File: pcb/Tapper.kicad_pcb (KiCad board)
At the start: 2 copper layers, 87.1 x 56 mm, 61 parts, among them J1 Barrel_Jack, J2 Conn_01x06_MountingPin, J3 Conn_01x06_MountingPin, J4 Conn_01x06_MountingPin, J5 Conn_01x14, U1 L7805

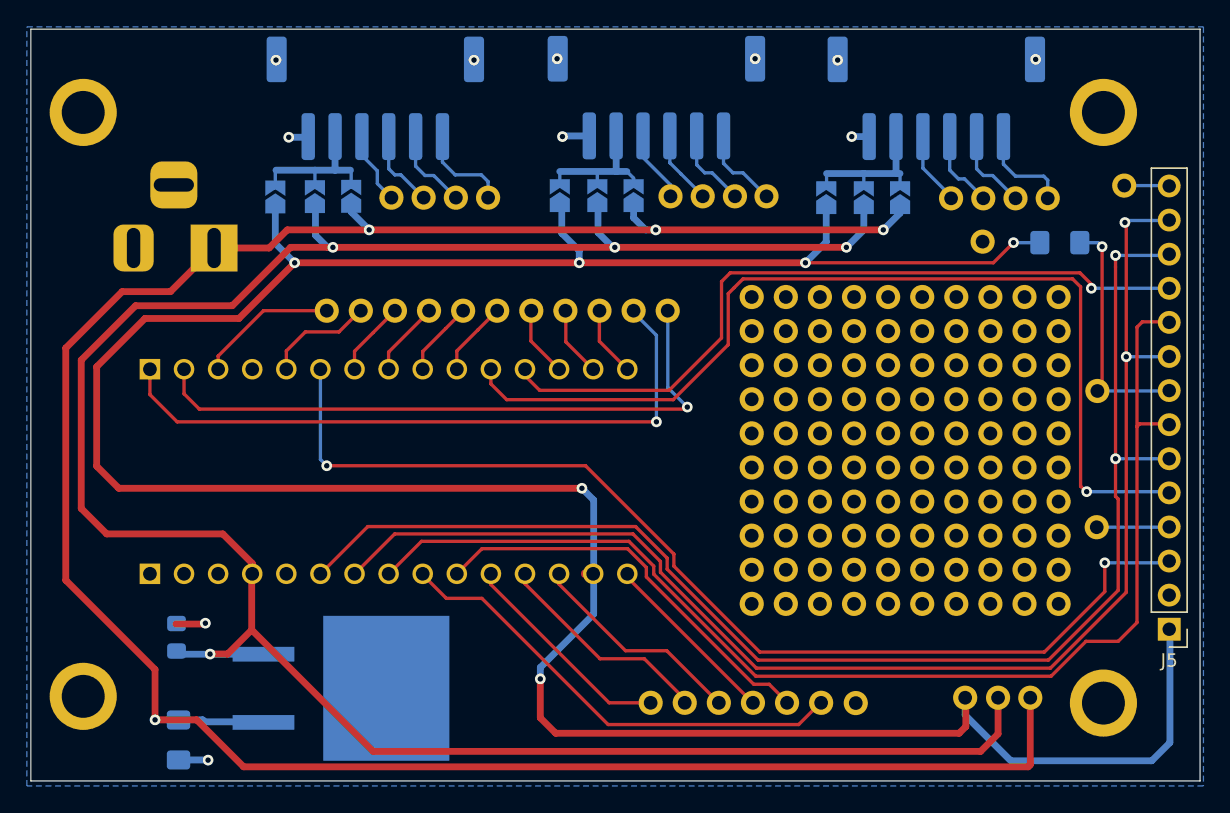
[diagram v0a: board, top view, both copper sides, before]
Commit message: Fix errors in rev1
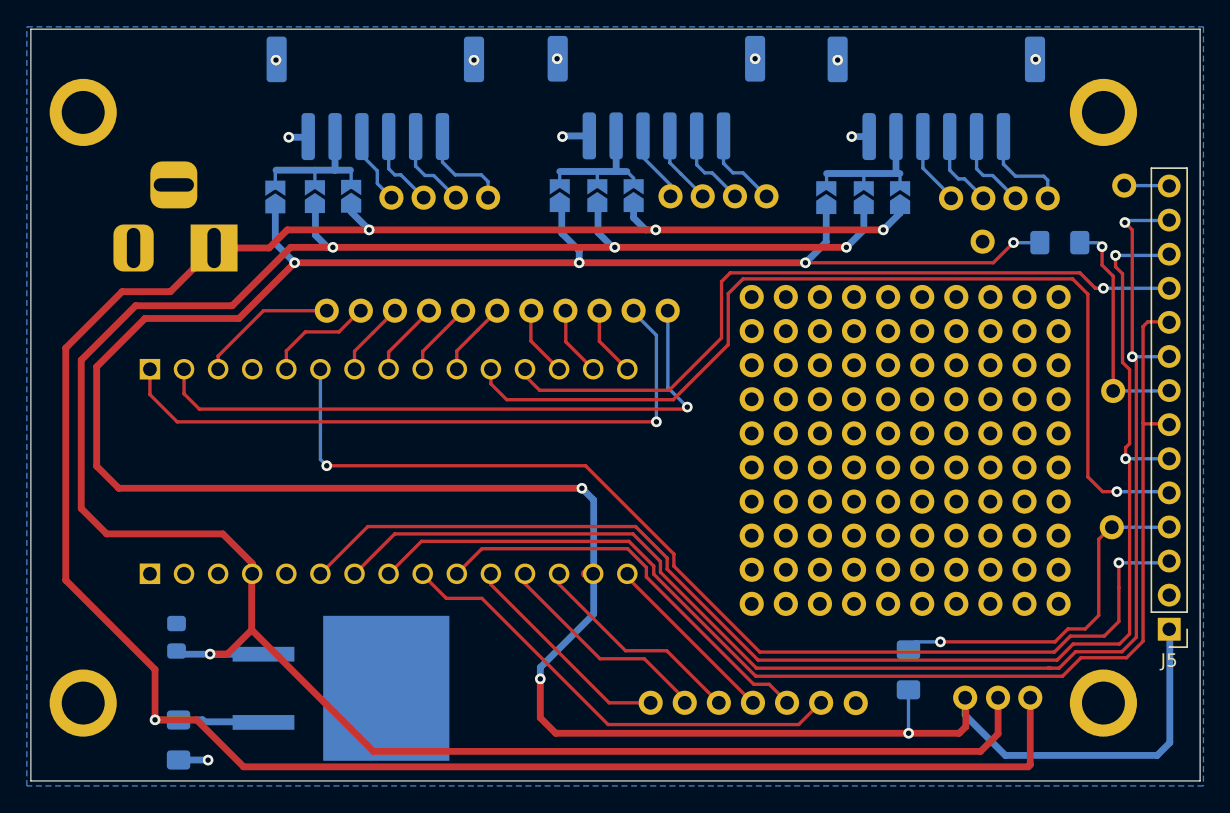
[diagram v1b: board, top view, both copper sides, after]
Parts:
- added R2: 10k, Resistor_SMD:R_1206_3216Metric_Pad1.42x1.75mm_HandSolder, B.Cu at (211.0, 91.5)
- moved TP5 1.17 mm to (226.2, 70.8)
- moved TP10 1.12 mm to (226.1, 80.9)
- moved H3 0.50 mm to (149.5, 94.0)
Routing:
- net /DISP_RST: track 5.40 -> 26.6 mm, vias 0 -> 1
- net +3V3: track 213.6 -> 216.5 mm, vias 6 -> 7
- net /DISP_MISO: track 99.8 -> 102.7 mm
- net /DISP_MOSI: track 100.7 -> 103.3 mm
- net GND: track 9.20 -> 6.98 mm, vias 11 -> 10
- net /DISP_CS: track 80.3 -> 81.6 mm
- net /DISP_LED: track 18.1 -> 17.1 mm
- net /DISP_DC: track 73.3 -> 72.6 mm
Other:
- board text added: "IRQ"
- board text added: "Tapper rev 2"
- board text removed: "Tapper rev 1, Oct 2020"
